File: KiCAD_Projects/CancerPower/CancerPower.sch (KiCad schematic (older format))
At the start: 25 parts, among them P1 CONN_01X01, P2 CONN_01X01, P3 CONN_01X01, P4 CONN_01X01, P5 CONN_01X02, P6 CONN_01X02, P7 CONN_01X04, P8 CONN_01X02, Q1 MOSFET_N, Q2 MOSFET_N, U1 V23076-D3001-D142, U2 MC78L05AACP

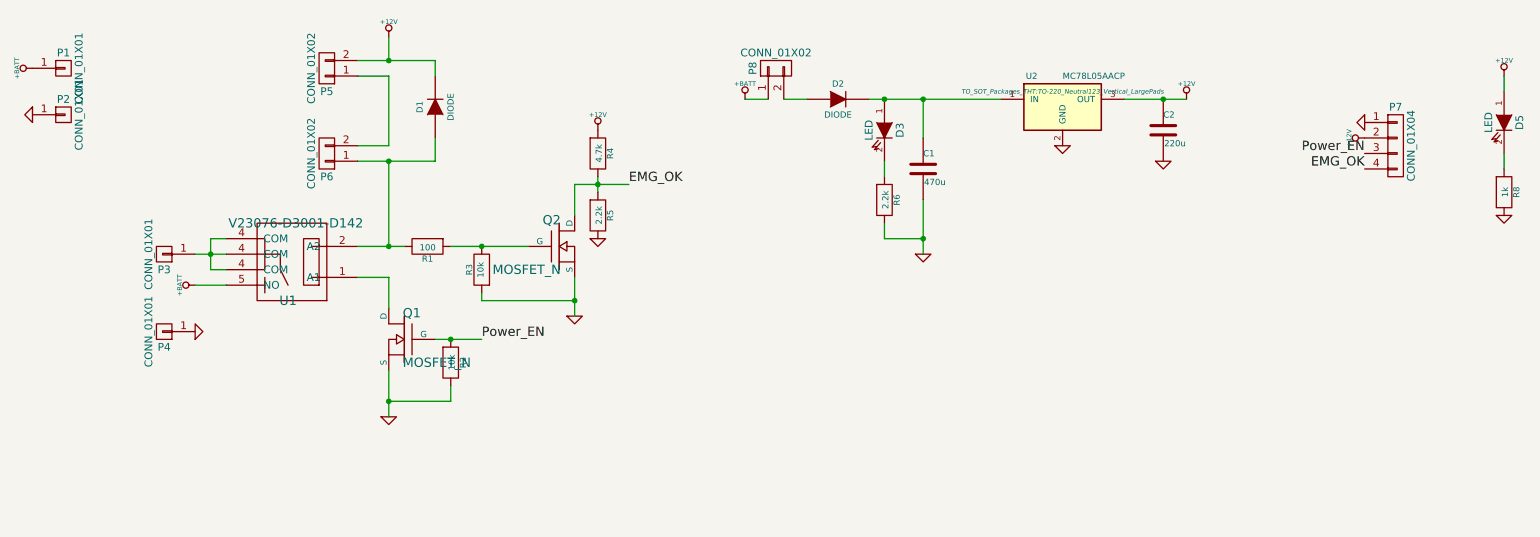
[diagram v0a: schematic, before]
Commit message: 明日の加工用データの出力､Cancer用電源基板の再設計
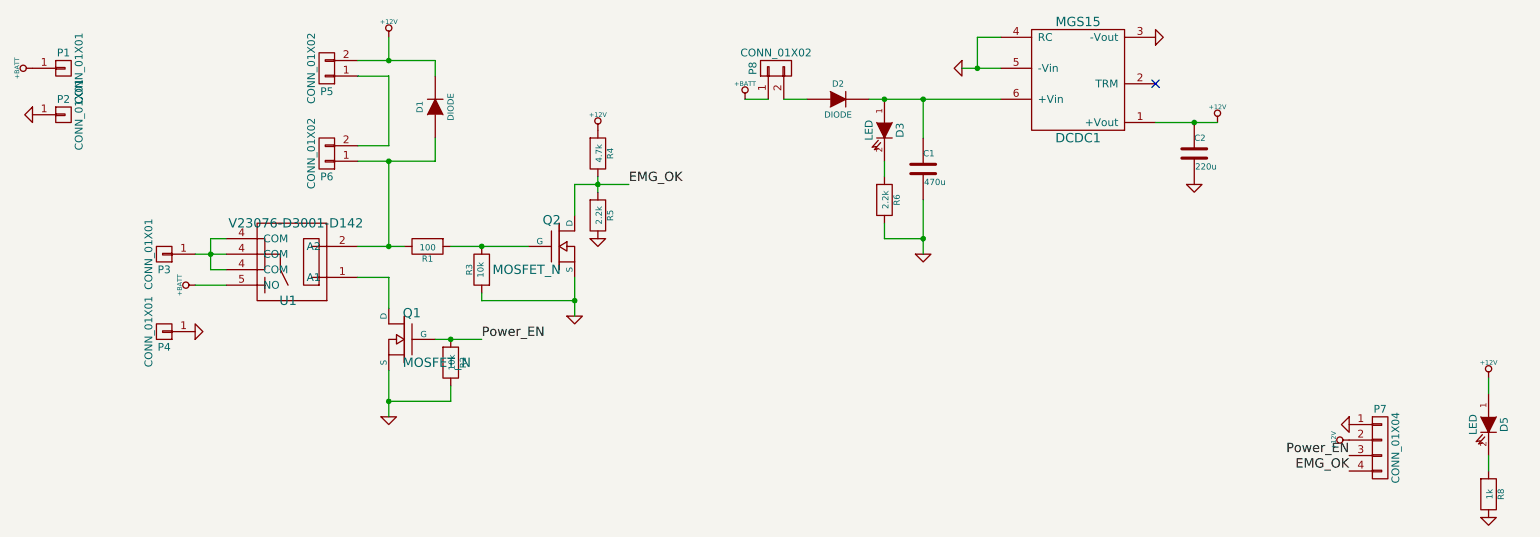
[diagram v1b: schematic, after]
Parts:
- removed U2: MC78L05AACP, TO_SOT_Packages_THT:TO-220_Neutral123_Vertical_LargePads, symbol MC78L05AACP
- added DCDC1: MGS15, RP_KiCAD_Libs:MGS15, symbol MGS15
- R2, R3, R4, R5, R6, R8: footprint RP_KiCAD_Libs:C1608_WP -> RP_KiCAD_Libs:C1608_NP
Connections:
- net +12V: now also DCDC1.1 (+Vout)
- net GND: now also DCDC1.3 (-Vout), DCDC1.4 (RC), DCDC1.5 (-Vin)
- net at C1.1, D2.1 (K), D3.1 (A): now also DCDC1.6 (+Vin)
- no-connect marks 0 -> 1
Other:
- moved on the sheet: C2, D5, P7, R8
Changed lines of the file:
@@
 	2450 2450 2250 2450
-$Comp
-L MC78L05AACP U2
-U 1 1 58B2A8AE
-P 7850 1300
-F 0 "U2" H 7650 1500 40  0000 C CNN
-F 1 "MC78L05AACP" H 7850 1500 40  0000 L CNN
-F 2 "TO_SOT_Packages_THT:TO-220_Neutral123_Vertical_LargePads" H 7850 1400 30  0000 C CIN
-F 3 "" H 7850 1300 60  0000 C CNN
-	1    7850 1300
-	1    0    0    -1
-$EndComp
 $Comp
 L CONN_01X02 P6
@@
 Connection ~ 6950 1250
 Wire Wire Line
-	8250 1250 8650 1250
+	8450 1400 8850 1400
 $Comp
 L GND #PWR07
 U 1 1 58B2BB65
-P 7850 1550
-F 0 "#PWR07" H 7850 1550 30  0001 C CNN
-F 1 "GND" H 7850 1480 30  0001 C CNN
-F 2 "" H 7850 1550 60  0001 C CNN
-F 3 "" H 7850 1550 60  0001 C CNN
-	1    7850 1550
-	1    0    0    -1
+P 7200 1050
+F 0 "#PWR07" H 7200 1050 30  0001 C CNN
+F 1 "GND" H 7200 980 30  0001 C CNN
+F 2 "" H 7200 1050 60  0001 C CNN
+F 3 "" H 7200 1050 60  0001 C CNN
+	1    7200 1050
+	0    1    1    0
 $EndComp
 $Comp
@@
 L C C2
 U 1 1 58B2BCEF
-P 8500 1450
-F 0 "C2" H 8500 1550 40  0000 L CNN
-F 1 "220u" H 8506 1365 40  0000 L CNN
-F 2 "Capacitors_ThroughHole:C_Radial_D6.3_L11.2_P2.5" H 8538 1300 30  0001 C CNN
-F 3 "" H 8500 1450 60  0000 C CNN
-	1    8500 1450
-	1    0    0    -1
-$EndComp
-Connection ~ 8500 1250
+P 8700 1600
+F 0 "C2" H 8700 1700 40  0000 L CNN
+F 1 "220u" H 8706 1515 40  0000 L CNN
+F 2 "Capacitors_ThroughHole:C_Radial_D6.3_L11.2_P2.5" H 8738 1450 30  0001 C CNN
+F 3 "" H 8700 1600 60  0000 C CNN
+	1    8700 1600
+	1    0    0    -1
+$EndComp
+Connection ~ 8700 1400
 $Comp
 L GND #PWR09
 U 1 1 58B2BE89
-P 8500 1650
-F 0 "#PWR09" H 8500 1650 30  0001 C CNN
-F 1 "GND" H 8500 1580 30  0001 C CNN
-F 2 "" H 8500 1650 60  0001 C CNN
-F 3 "" H 8500 1650 60  0001 C CNN
-	1    8500 1650
+P 8700 1800
+F 0 "#PWR09" H 8700 1800 30  0001 C CNN
+F 1 "GND" H 8700 1730 30  0001 C CNN
+F 2 "" H 8700 1800 60  0001 C CNN
+F 3 "" H 8700 1800 60  0001 C CNN
+	1    8700 1800
 	1    0    0    -1
 $EndComp
@@
 L +12V #PWR010
 U 1 1 58B2BF92
-P 8650 1250
-F 0 "#PWR010" H 8650 1200 20  0001 C CNN
-F 1 "+12V" H 8650 1350 30  0000 C CNN
-F 2 "" H 8650 1250 60  0001 C CNN
-F 3 "" H 8650 1250 60  0001 C CNN
-	1    8650 1250
+P 8850 1400
+F 0 "#PWR010" H 8850 1350 20  0001 C CNN
+F 1 "+12V" H 8850 1500 30  0000 C CNN
+F 2 "" H 8850 1400 60  0001 C CNN
+F 3 "" H 8850 1400 60  0001 C CNN
+	1    8850 1400
 	1    0    0    -1
 $EndComp
@@
 F 0 "R6" V 6780 1900 40  0000 C CNN
 F 1 "2.2k" V 6707 1901 40  0000 C CNN
-F 2 "RP_KiCAD_Libs:C1608_WP" V 6630 1900 30  0001 C CNN
+F 2 "RP_KiCAD_Libs:C1608_NP" V 6630 1900 30  0001 C CNN
 F 3 "" H 6700 1900 30  0000 C CNN
 	1    6700 1900
@@
 L CONN_01X04 P7
 U 1 1 58B2CD26
-P 10000 1550
-F 0 "P7" H 10000 1800 50  0000 C CNN
-F 1 "CONN_01X04" V 10100 1550 50  0000 C CNN
-F 2 "RP_KiCAD_Connector:XA_4LC" H 10000 1550 50  0001 C CNN
-F 3 "" H 10000 1550 50  0000 C CNN
-	1    10000 1550
+P 9900 3500
+F 0 "P7" H 9900 3750 50  0000 C CNN
+F 1 "CONN_01X04" V 10000 3500 50  0000 C CNN
+F 2 "RP_KiCAD_Connector:XA_4LC" H 9900 3500 50  0001 C CNN
+F 3 "" H 9900 3500 50  0000 C CNN
+	1    9900 3500
 	1    0    0    -1
 $EndComp
@@
 L +12V #PWR011
 U 1 1 58B2CFE0
-P 9800 1500
-F 0 "#PWR011" H 9800 1450 20  0001 C CNN
-F 1 "+12V" H 9800 1600 30  0000 C CNN
-F 2 "" H 9800 1500 60  0001 C CNN
-F 3 "" H 9800 1500 60  0001 C CNN
-	1    9800 1500
+P 9700 3450
+F 0 "#PWR011" H 9700 3400 20  0001 C CNN
+F 1 "+12V" H 9700 3550 30  0000 C CNN
+F 2 "" H 9700 3450 60  0001 C CNN
+F 3 "" H 9700 3450 60  0001 C CNN
+	1    9700 3450
 	0    -1   -1   0
 $EndComp
@@
 L GND #PWR012
 U 1 1 58B2D01E
-P 9800 1400
-F 0 "#PWR012" H 9800 1400 30  0001 C CNN
-F 1 "GND" H 9800 1330 30  0001 C CNN
-F 2 "" H 9800 1400 60  0001 C CNN
-F 3 "" H 9800 1400 60  0001 C CNN
-	1    9800 1400
+P 9700 3350
+F 0 "#PWR012" H 9700 3350 30  0001 C CNN
+F 1 "GND" H 9700 3280 30  0001 C CNN
+F 2 "" H 9700 3350 60  0001 C CNN
+F 3 "" H 9700 3350 60  0001 C CNN
+	1    9700 3350
 	0    1    1    0
 $EndComp
@@
 L LED D5
 U 1 1 58B2DEA2
-P 10700 1400
-F 0 "D5" H 10700 1500 50  0000 C CNN
-F 1 "LED" H 10700 1300 50  0000 C CNN
-F 2 "LEDs:LED-3MM" H 10700 1400 60  0001 C CNN
-F 3 "" H 10700 1400 60  0000 C CNN
-	1    10700 1400
+P 10600 3350
+F 0 "D5" H 10600 3450 50  0000 C CNN
+F 1 "LED" H 10600 3250 50  0000 C CNN
+F 2 "LEDs:LED-3MM" H 10600 3350 60  0001 C CNN
+F 3 "" H 10600 3350 60  0000 C CNN
+	1    10600 3350
 	0    1    1    0
 $EndComp
@@
 L R R8
 U 1 1 58B2DEA8
-P 10700 1850
-F 0 "R8" V 10780 1850 40  0000 C CNN
-F 1 "1k" V 10707 1851 40  0000 C CNN
-F 2 "RP_KiCAD_Libs:C1608_WP" V 10630 1850 30  0001 C CNN
-F 3 "" H 10700 1850 30  0000 C CNN
-	1    10700 1850
+P 10600 3800
+F 0 "R8" V 10680 3800 40  0000 C CNN
+F 1 "1k" V 10607 3801 40  0000 C CNN
+F 2 "RP_KiCAD_Libs:C1608_NP" V 10530 3800 30  0001 C CNN
+F 3 "" H 10600 3800 30  0000 C CNN
+	1    10600 3800
 	1    0    0    -1
 $EndComp
@@
 L GND #PWR013
 U 1 1 58B2DEAE
-P 10700 2000
-F 0 "#PWR013" H 10700 2000 30  0001 C CNN
-F 1 "GND" H 10700 1930 30  0001 C CNN
-F 2 "" H 10700 2000 60  0001 C CNN
-F 3 "" H 10700 2000 60  0001 C CNN
-	1    10700 2000
-	1    0    0    -1
-$EndComp
-Wire Wire Line
-	10700 1600 10700 1700
-Wire Wire Line
-	10700 1100 10700 1200
+P 10600 3950
+F 0 "#PWR013" H 10600 3950 30  0001 C CNN
+F 1 "GND" H 10600 3880 30  0001 C CNN
+F 2 "" H 10600 3950 60  0001 C CNN
+F 3 "" H 10600 3950 60  0001 C CNN
+	1    10600 3950
+	1    0    0    -1
+$EndComp
+Wire Wire Line
+	10600 3550 10600 3650
+Wire Wire Line
+	10600 3050 10600 3150
 $Comp
 L +12V #PWR014
 U 1 1 58B2E37D
-P 10700 1100
-F 0 "#PWR014" H 10700 1050 20  0001 C CNN
-F 1 "+12V" H 10700 1200 30  0000 C CNN
-F 2 "" H 10700 1100 60  0001 C CNN
-F 3 "" H 10700 1100 60  0001 C CNN
-	1    10700 1100
+P 10600 3050
+F 0 "#PWR014" H 10600 3000 20  0001 C CNN
+F 1 "+12V" H 10600 3150 30  0000 C CNN
+F 2 "" H 10600 3050 60  0001 C CNN
+F 3 "" H 10600 3050 60  0001 C CNN
+	1    10600 3050
 	1    0    0    -1
 $EndComp
@@
 F 0 "R2" V 3980 2950 40  0000 C CNN
 F 1 "10k" V 3907 2951 40  0000 C CNN
-F 2 "RP_KiCAD_Libs:C1608_WP" V 3830 2950 30  0001 C CNN
+F 2 "RP_KiCAD_Libs:C1608_NP" V 3830 2950 30  0001 C CNN
 F 3 "" H 3900 2950 30  0000 C CNN
 	1    3900 2950
@@
 F 0 "R3" V 4180 2350 40  0000 C CNN
 F 1 "10k" V 4107 2351 40  0000 C CNN
-F 2 "RP_KiCAD_Libs:C1608_WP" V 4030 2350 30  0001 C CNN
+F 2 "RP_KiCAD_Libs:C1608_NP" V 4030 2350 30  0001 C CNN
 F 3 "" H 4100 2350 30  0000 C CNN
 	1    4100 2350
@@
 Connection ~ 4100 2200
 Connection ~ 3500 2200
-Text Label 9800 1600 2    60   ~ 0
+Text Label 9700 3550 2    60   ~ 0
 Power_EN
 $Comp
@@
 F 0 "R4" V 4930 1600 40  0000 C CNN
 F 1 "4.7k" V 4857 1601 40  0000 C CNN
-F 2 "RP_KiCAD_Libs:C1608_WP" V 4780 1600 30  0001 C CNN
+F 2 "RP_KiCAD_Libs:C1608_NP" V 4780 1600 30  0001 C CNN
 F 3 "" H 4850 1600 30  0000 C CNN
 	1    4850 1600
@@
 F 0 "R5" V 4930 2000 40  0000 C CNN
 F 1 "2.2k" V 4857 2001 40  0000 C CNN
-F 2 "RP_KiCAD_Libs:C1608_WP" V 4780 2000 30  0001 C CNN
+F 2 "RP_KiCAD_Libs:C1608_NP" V 4780 2000 30  0001 C CNN
 F 3 "" H 4850 2000 30  0000 C CNN
 	1    4850 2000
@@
 Text Label 5050 1800 0    60   ~ 0
 EMG_OK
-Text Label 9800 1700 2    60   ~ 0
+Text Label 9700 3650 2    60   ~ 0
 EMG_OK
 $Comp
@@
 Wire Wire Line
 	6200 1250 6050 1250
+$Comp
+L MGS15 DCDC1
+U 1 1 58DE1A40
+P 7950 1050
+F 0 "DCDC1" H 7950 1500 60  0000 C CNN
+F 1 "MGS15" H 7950 750 60  0000 C CNN
+F 2 "RP_KiCAD_Libs:MGS15" H 7950 1050 60  0001 C CNN
+F 3 "" H 7950 1050 60  0001 C CNN
+	1    7950 1050
+	-1   0    0    1
+$EndComp
+Wire Wire Line
+	7200 1050 7450 1050
+Wire Wire Line
+	7450 850  7300 850
+Wire Wire Line
+	7300 850  7300 1050
+Connection ~ 7300 1050
+NoConn ~ 8450 1150
+$Comp
+L GND #PWR019
+U 1 1 58DE2636
+P 8450 850
+F 0 "#PWR019" H 8450 850 30  0001 C CNN
+F 1 "GND" H 8450 780 30  0001 C CNN
+F 2 "" H 8450 850 60  0001 C CNN
+F 3 "" H 8450 850 60  0001 C CNN
+	1    8450 850
+	0    -1   -1   0
+$EndComp
 $EndSCHEMATC
